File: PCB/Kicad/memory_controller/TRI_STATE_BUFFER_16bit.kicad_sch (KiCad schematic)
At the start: 4 parts, among them U1 74LS245, U2 74LS245

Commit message: fix
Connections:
- net nOE renamed ~{OE}
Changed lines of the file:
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@@
 		)
 	)
-	(hierarchical_label "nOE"
+	(hierarchical_label "~{OE}"
 		(shape input)
 		(at 107.95 93.98 180)
@@
 		)
 	)
-	(hierarchical_label "nOE"
+	(hierarchical_label "~{OE}"
 		(shape input)
 		(at 106.68 148.59 180)
@@
 					(unit 1)
 				)
-				(path "/dccec861-b967-466c-843e-d6d1ad6064ce/99641bee-a21b-44b3-bb6c-fba4081b468d"
-					(reference "C13")
-					(unit 1)
-				)
 			)
 		)
@@
 					(unit 1)
 				)
-				(path "/dccec861-b967-466c-843e-d6d1ad6064ce/99641bee-a21b-44b3-bb6c-fba4081b468d"
-					(reference "U14")
-					(unit 1)
-				)
 			)
 		)
@@
 					(unit 1)
 				)
-				(path "/dccec861-b967-466c-843e-d6d1ad6064ce/99641bee-a21b-44b3-bb6c-fba4081b468d"
-					(reference "#PWR068")
-					(unit 1)
-				)
 			)
 		)
@@
 					(unit 1)
 				)
-				(path "/dccec861-b967-466c-843e-d6d1ad6064ce/99641bee-a21b-44b3-bb6c-fba4081b468d"
-					(reference "#PWR069")
-					(unit 1)
-				)
 			)
 		)
@@
 					(unit 1)
 				)
-				(path "/dccec861-b967-466c-843e-d6d1ad6064ce/99641bee-a21b-44b3-bb6c-fba4081b468d"
-					(reference "C14")
-					(unit 1)
-				)
 			)
 		)
@@
 					(unit 1)
 				)
-				(path "/dccec861-b967-466c-843e-d6d1ad6064ce/99641bee-a21b-44b3-bb6c-fba4081b468d"
-					(reference "#PWR066")
-					(unit 1)
-				)
 			)
 		)
@@
 					(unit 1)
 				)
-				(path "/dccec861-b967-466c-843e-d6d1ad6064ce/99641bee-a21b-44b3-bb6c-fba4081b468d"
-					(reference "#PWR070")
-					(unit 1)
-				)
 			)
 		)
@@
 					(unit 1)
 				)
-				(path "/dccec861-b967-466c-843e-d6d1ad6064ce/99641bee-a21b-44b3-bb6c-fba4081b468d"
-					(reference "#PWR065")
-					(unit 1)
-				)
 			)
 		)
@@
 					(unit 1)
 				)
-				(path "/dccec861-b967-466c-843e-d6d1ad6064ce/99641bee-a21b-44b3-bb6c-fba4081b468d"
-					(reference "U13")
-					(unit 1)
-				)
 			)
 		)
@@
 					(unit 1)
 				)
-				(path "/dccec861-b967-466c-843e-d6d1ad6064ce/99641bee-a21b-44b3-bb6c-fba4081b468d"
-					(reference "#PWR067")
-					(unit 1)
-				)
 			)
 		)
@@
 					(unit 1)
 				)
-				(path "/dccec861-b967-466c-843e-d6d1ad6064ce/99641bee-a21b-44b3-bb6c-fba4081b468d"
-					(reference "#PWR072")
-					(unit 1)
-				)
 			)
 		)
@@
 					(unit 1)
 				)
-				(path "/dccec861-b967-466c-843e-d6d1ad6064ce/99641bee-a21b-44b3-bb6c-fba4081b468d"
-					(reference "#PWR073")
-					(unit 1)
-				)
 			)
 		)
@@
 					(unit 1)
 				)
-				(path "/dccec861-b967-466c-843e-d6d1ad6064ce/99641bee-a21b-44b3-bb6c-fba4081b468d"
-					(reference "#PWR071")
-					(unit 1)
-				)
 			)
 		)
@@
 					(unit 1)
 				)
-				(path "/dccec861-b967-466c-843e-d6d1ad6064ce/99641bee-a21b-44b3-bb6c-fba4081b468d"
-					(reference "#PWR074")
-					(unit 1)
-				)

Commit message: pcb init
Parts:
- C1, C2: footprint (none) -> Capacitor_SMD:C_0402_1005Metric
- U1, U2: footprint (none) -> Package_SO:SOIC-20W_7.5x12.8mm_P1.27mm
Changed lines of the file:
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@@
 			)
 		)
-		(property "Footprint" ""
+		(property "Footprint" "Capacitor_SMD:C_0402_1005Metric"
 			(at 142.5448 93.98 0)
 			(effects
@@
 			)
 		)
-		(property "Footprint" ""
+		(property "Footprint" "Package_SO:SOIC-20W_7.5x12.8mm_P1.27mm"
 			(at 125.73 135.89 0)
 			(effects
@@
 			)
 		)
-		(property "Footprint" ""
+		(property "Footprint" "Capacitor_SMD:C_0402_1005Metric"
 			(at 143.8148 151.13 0)
 			(effects
@@
 			)
 		)
-		(property "Footprint" ""
+		(property "Footprint" "Package_SO:SOIC-20W_7.5x12.8mm_P1.27mm"
 			(at 125.73 81.28 0)
 			(effects

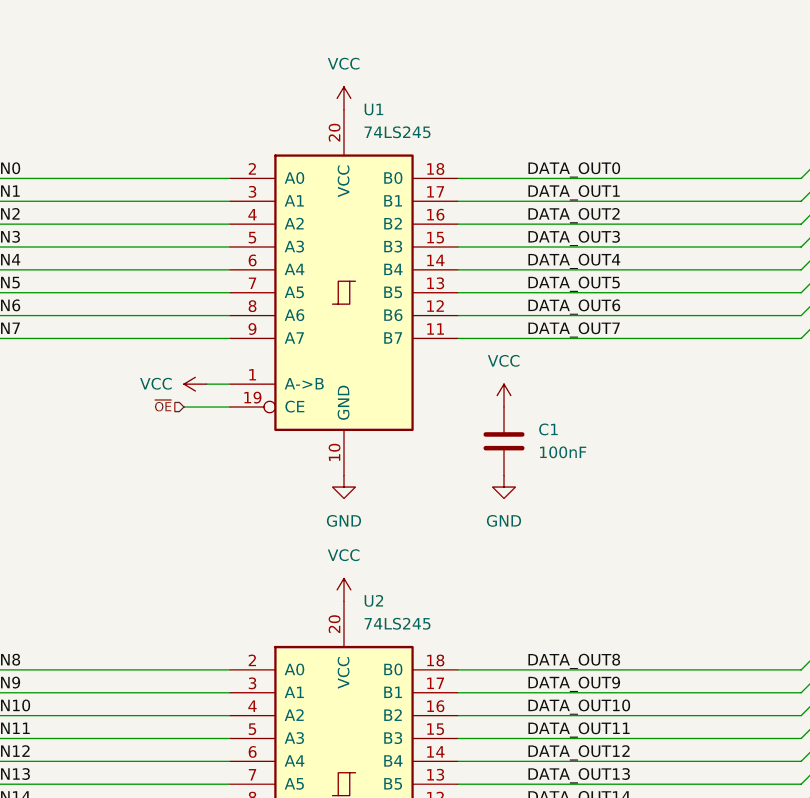
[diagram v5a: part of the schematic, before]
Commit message: memory controller schematic update
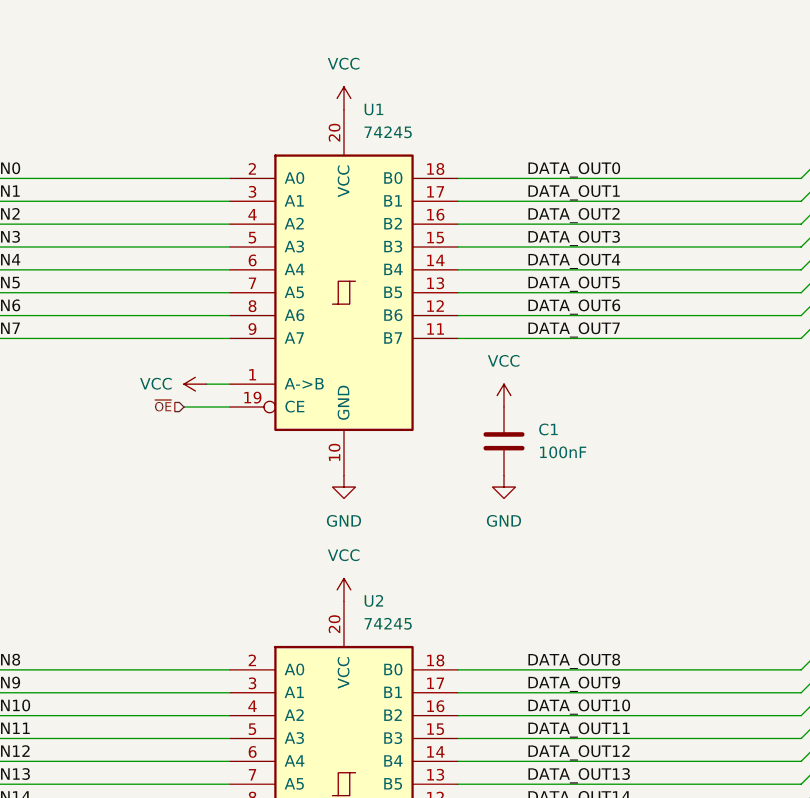
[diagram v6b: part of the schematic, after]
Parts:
- U1, U2: value 74LS245 -> 74245; footprint Package_SO:SOIC-20W_7.5x12.8mm_P1.27mm -> Package_SO:TSSOP-20_4.4x6.5mm_P0.65mm
